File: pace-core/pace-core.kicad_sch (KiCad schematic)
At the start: 3 parts, among them U1 ESP32-S3-WROOM-1

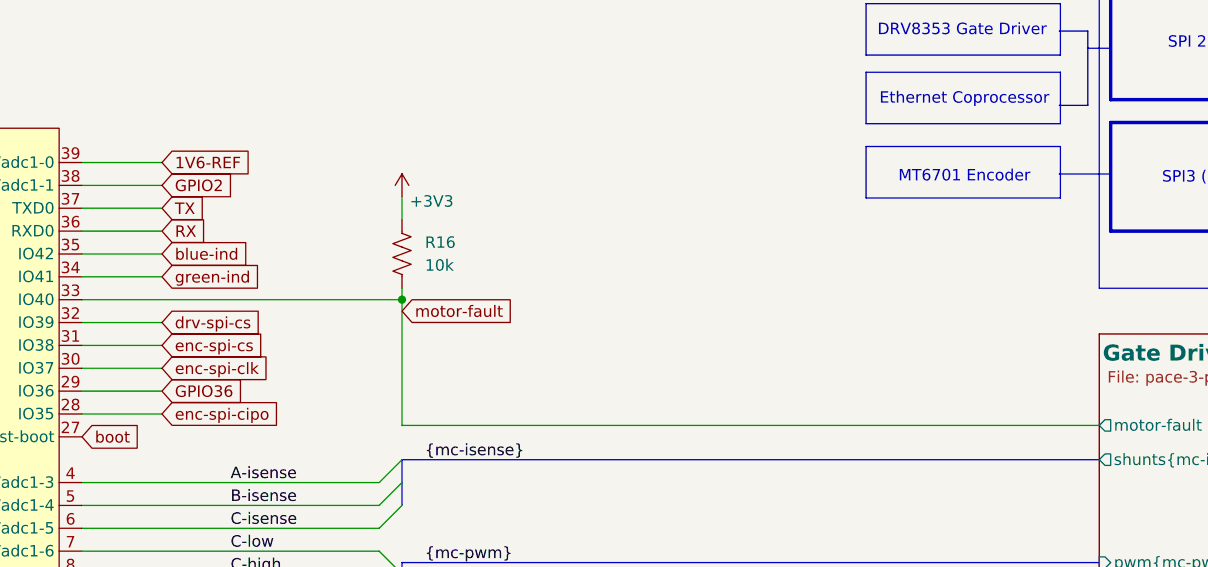
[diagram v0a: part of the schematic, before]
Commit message: design checkpoint: v1 repackage — new connectors, footprints, and layout updates
- Add JST SH/SR series, XT30PW-M, TH cap, and SOT-23-3 footprints with 3D models
- Update connectors, power-reg, and mechanicals schematic sheets
- Rework PCB layout and update board STEP exports (r0 updated, r2 added)
- Regenerate interactive BOM

Co-Authored-By: Claude Fable 5 <noreply@anthropic.com>
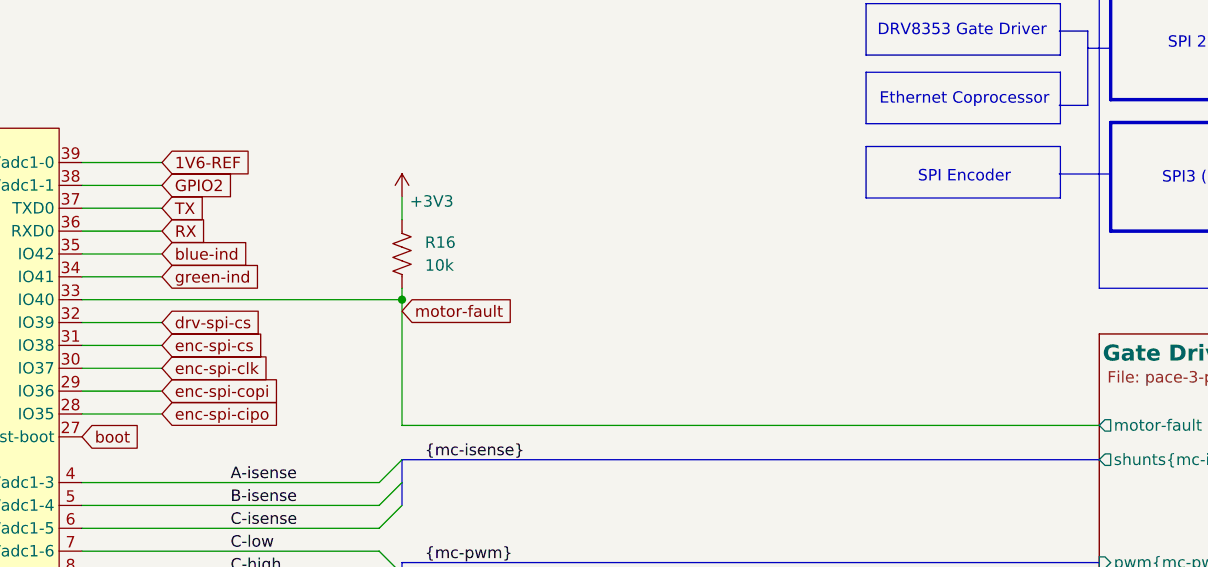
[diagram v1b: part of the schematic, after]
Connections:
- net GPIO36 renamed enc-spi-copi
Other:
- note added: "SPI Encoder"
- note removed: "MT6701 Encoder"
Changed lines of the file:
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@@
 		)
 	)
-	(text "MT6701 Encoder"
+	(text "SPI Encoder"
 		(exclude_from_sim no)
 		(at 184.404 41.021 0)
@@
 		)
 	)
-	(global_label "GPIO36"
+	(global_label "enc-spi-copi"
 		(shape input)
 		(at 95.25 64.77 0)
@@
 		)
 		(property "Intersheetrefs" "${INTERSHEET_REFS}"
-			(at 105.1295 64.77 0)
+			(at 111.4795 64.77 0)
 			(hide yes)
 			(show_name no)

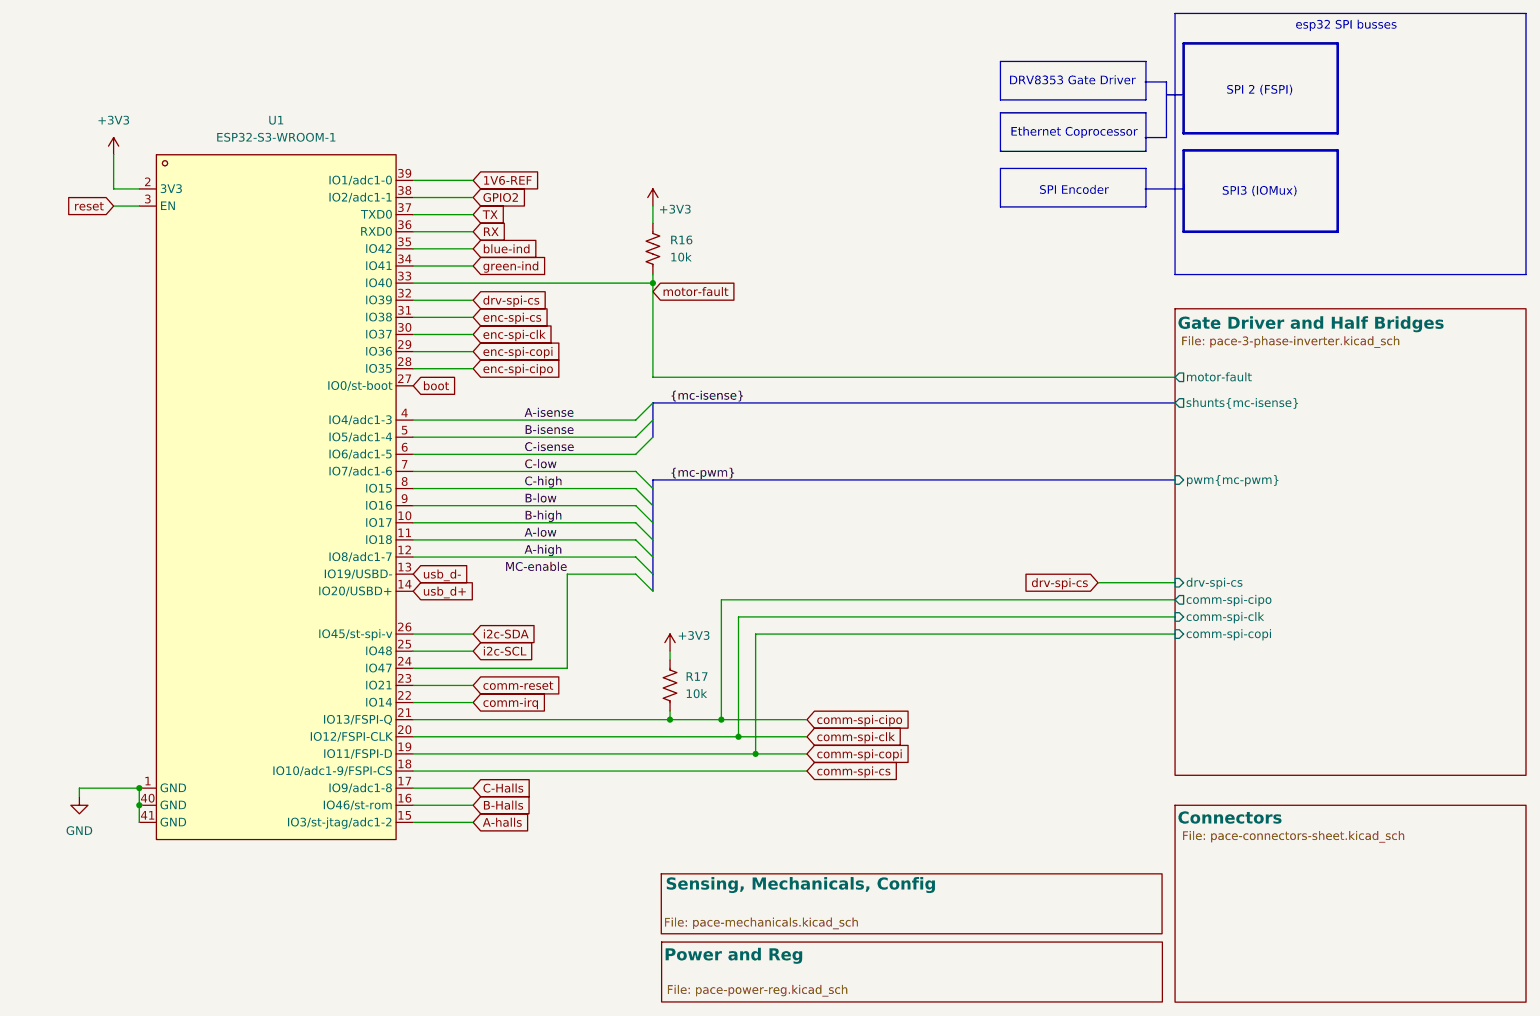
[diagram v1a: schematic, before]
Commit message: Repo hygiene, CI as source of truth, and V1R2 design cleanup
Repository
- Sources only in pace-core/: untrack .history, lock files, .DS_Store,
  backups, layer PDFs, STEP exports, ibom. Regenerable outputs are
  gitignored; CI rebuilds them.
- Git LFS for Blender, PSD, video and curated renders (.gitattributes).
- Move brand artwork to graphics/, curated renders to docs/media/.
- Track the V1R2 fab package CSVs that the old gitignore hid.

CI
- KiBot builds gerbers, drill, fab zip, BOM (CSV/HTML with MPN and LCSC),
  position, ibom, IPC netlist, schematic and layer PDFs, DRC report,
  STEP and renders. REV is set from `git describe` on V*R* tags.
- ERC and DRC block PRs; tag builds publish a GitHub Release.
- README pin map is generated from the netlist (tools/gen_readme.py)
  and checked in CI.
- PR template with review checklist.

Design (ERC 0 errors, DRC 0 errors with schematic parity, netlist
connectivity verified identical across all 101 nets)
- Rename 49 nets to lowercase domain-kebab via tools/rename_nets.py.
- Add TITLE/PROJECT_CODE/REV/COMPANY text variables and title blocks on
  every sheet and the board.
- Net classes now carry both widths and colours: GND, 3V3, 5V, GND-USB,
  Batt, Motor-A/B/C. Remove High-Current-GND (its net never existed).
- Remove all 10 stale DRC exclusions; fold the shunt net-tie bridge copper
  into pad 2 and waive clearance around NT1..NT3 via pace-core.kicad_dru.
- Add Manufacturer/MPN/LCSC fields to every symbol and footprint.
- Fix capacitor symbols with input-typed pins, add PWR_FLAGs on GND and
  +BATT, convert duplicate local labels to global, complete the
  half-bridge bus alias, re-home symbols from missing libraries.

Docs
- docs/style-guide.md, decision records 0001-0003, errata, bring-up
  checklist. CLAUDE.md updated for the new layout and conventions.

Co-Authored-By: Claude Fable 5.1 <noreply@anthropic.com>
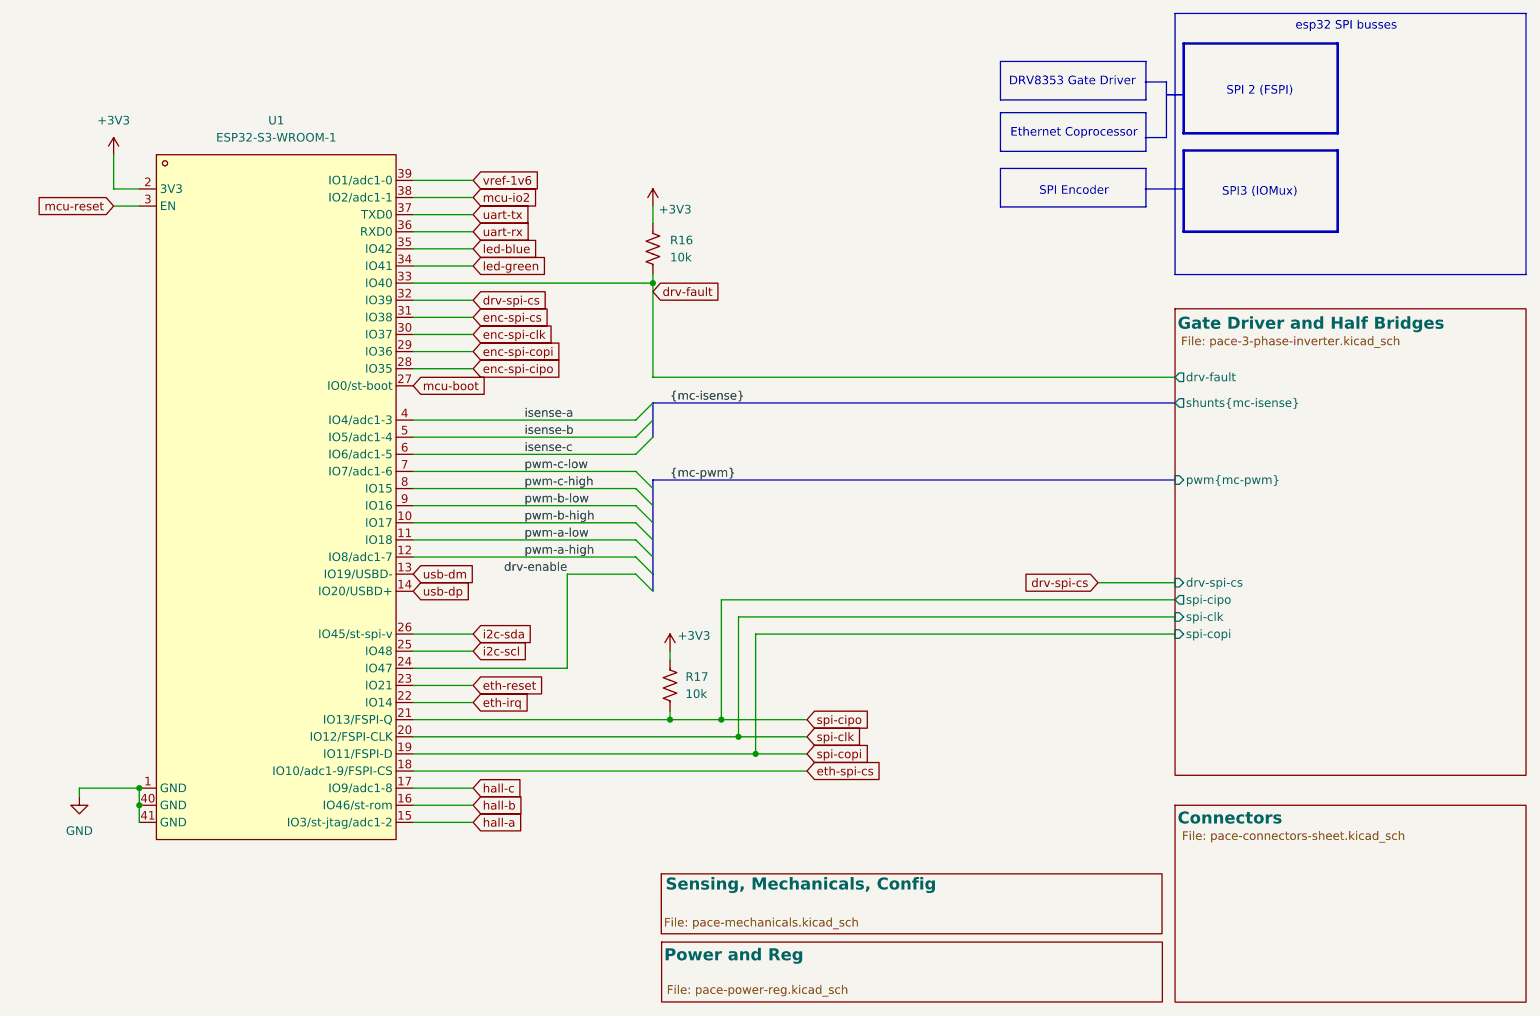
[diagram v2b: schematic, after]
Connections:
- net 1V6-REF renamed vref-1v6
- net A-halls renamed hall-a
- net A-high renamed pwm-a-high
- net A-isense renamed isense-a
- net A-low renamed pwm-a-low
- net B-Halls renamed hall-b
- net B-high renamed pwm-b-high
- net B-isense renamed isense-b
- net B-low renamed pwm-b-low
- net C-Halls renamed hall-c
- net C-high renamed pwm-c-high
- net C-isense renamed isense-c
- net C-low renamed pwm-c-low
- net GPIO2 renamed mcu-io2
- net MC-enable renamed drv-enable
- net RX renamed uart-rx
- net TX renamed uart-tx
- net blue-ind renamed led-blue
- net boot renamed mcu-boot
- net comm-irq renamed eth-irq
- net comm-reset renamed eth-reset
- net comm-spi-cipo renamed spi-cipo
- net comm-spi-clk renamed spi-clk
- net comm-spi-copi renamed spi-copi
- net comm-spi-cs renamed eth-spi-cs
- net green-ind renamed led-green
- net i2c-SCL renamed i2c-scl
- net i2c-SDA renamed i2c-sda
- net motor-fault renamed drv-fault
- net reset renamed mcu-reset
- net usb_d+ renamed usb-dp
- net usb_d- renamed usb-dm
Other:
- sheet Gate Driver and Half Bridges ports: added drv-fault, spi-cipo, spi-clk, spi-copi; removed comm-spi-cipo, comm-spi-clk, comm-spi-copi, motor-fault
- company: (none) -> ${COMPANY}
- title: (none) -> ${TITLE} - System
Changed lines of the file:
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@@
 	(generator_version "10.0")
 	(paper "A4")
+	(title_block
+		(title "${TITLE} - System")
+		(date "2026-09-30")
+		(rev "${REV}")
+		(company "${COMPANY}")
+		(comment 1 "Root sheet: ESP32-S3 MCU, sheet interconnect, pin allocation")
+		(comment 2 "Project code ${PROJECT_CODE}")
+	)
 	(rectangle
 		(start 200.66 19.05)
@@
 		)
 	)
-	(label "A-isense"
+	(label "isense-a"
 		(at 102.87 74.93 0)
 		(effects
@@
 		)
 	)
-	(label "B-isense"
+	(label "isense-b"
 		(at 102.87 77.47 0)
 		(effects
@@
 		)
 	)
-	(label "C-isense"
+	(label "isense-c"
 		(at 102.87 80.01 0)
 		(effects
@@
 		)
 	)
-	(label "A-low"
+	(label "pwm-a-low"
 		(at 102.87 92.71 0)
 		(effects
@@
 		)
 	)
-	(label "C-high"
+	(label "pwm-c-high"
 		(at 102.87 85.09 0)
 		(effects
@@
 		)
 	)
-	(label "C-low"
+	(label "pwm-c-low"
 		(at 102.87 82.55 0)
 		(effects
@@
 		)
 	)
-	(label "A-high"
+	(label "pwm-a-high"
 		(at 102.87 95.25 0)
 		(effects
@@
 		)
 	)
-	(label "MC-enable"
+	(label "drv-enable"
 		(at 109.22 97.79 180)
 		(effects
@@
 		)
 	)
-	(label "B-low"
+	(label "pwm-b-low"
 		(at 102.87 87.63 0)
 		(effects
@@
 		)
 	)
-	(label "B-high"
+	(label "pwm-b-high"
 		(at 102.87 90.17 0)
 		(effects
@@
 		)
 	)
-	(global_label "green-ind"
+	(global_label "led-green"
 		(shape input)
 		(at 95.25 52.07 0)
@@
 		)
 	)
-	(global_label "comm-spi-clk"
+	(global_label "spi-clk"
 		(shape input)
 		(at 144.78 121.92 0)
@@
 		)
 	)
-	(global_label "RX"
+	(global_label "uart-rx"
 		(shape input)
 		(at 95.25 46.99 0)
@@
 		)
 	)
-	(global_label "comm-spi-cipo"
+	(global_label "spi-cipo"
 		(shape input)
 		(at 144.78 119.38 0)
@@
 		)
 	)
-	(global_label "comm-reset"
+	(global_label "eth-reset"
 		(shape input)
 		(at 95.25 114.3 0)
@@
 		)
 	)
-	(global_label "comm-spi-cs"
+	(global_label "eth-spi-cs"
 		(shape input)
 		(at 144.78 127 0)
@@
 		)
 	)
-	(global_label "TX"
+	(global_label "uart-tx"
 		(shape input)
 		(at 95.25 44.45 0)
@@
 		)
 	)
-	(global_label "boot"
+	(global_label "mcu-boot"
 		(shape input)
 		(at 86.36 69.85 0)
@@
 		)
 	)
-	(global_label "B-Halls"
+	(global_label "hall-b"
 		(shape input)
 		(at 95.25 132.08 0)
@@
 		)
 	)
-	(global_label "usb_d+"
+	(global_label "usb-dp"
 		(shape input)
 		(at 86.36 100.33 0)
@@
 		)
 	)
-	(global_label "motor-fault"
+	(global_label "drv-fault"
 		(shape input)
 		(at 121.92 55.88 0)
@@
 		)
 	)
-	(global_label "reset"
+	(global_label "mcu-reset"
 		(shape input)
 		(at 41.91 43.18 180)
@@
 		)
 	)
-	(global_label "GPIO2"
+	(global_label "mcu-io2"
 		(shape input)
 		(at 95.25 41.91 0)
@@
 		)
 	)
-	(global_label "usb_d-"
+	(global_label "usb-dm"
 		(shape input)
 		(at 86.36 97.79 0)
@@
 		)
 	)
-	(global_label "A-halls"
+	(global_label "hall-a"
 		(shape input)
 		(at 95.25 134.62 0)
@@
 		)
 	)
-	(global_label "1V6-REF"
+	(global_label "vref-1v6"
 		(shape input)
 		(at 95.25 39.37 0)
@@
 		)
 	)
-	(global_label "i2c-SDA"
+	(global_label "i2c-sda"
 		(shape input)
 		(at 95.25 106.68 0)
@@
 		)
 	)
-	(global_label "comm-irq"
+	(global_label "eth-irq"
 		(shape input)
 		(at 95.25 116.84 0)
@@
 		)
 	)
-	(global_label "blue-ind"
+	(global_label "led-blue"
 		(shape input)
 		(at 95.25 49.53 0)
@@
 		)
 	)
-	(global_label "C-Halls"
+	(global_label "hall-c"
 		(shape input)
 		(at 95.25 129.54 0)
@@
 		)
 	)
-	(global_label "comm-spi-copi"
+	(global_label "spi-copi"
 		(shape input)
 		(at 144.78 124.46 0)
@@
 		)
 	)
-	(global_label "i2c-SCL"
+	(global_label "i2c-scl"
 		(shape input)
 		(at 95.25 109.22 0)
@@
 			)
 		)
+		(property "Manufacturer" ""
+			(at 121.92 49.53 0)
+			(show_name no)
+			(do_not_autoplace no)
+			(effects
+				(font
+					(size 1.27 1.27)
+				)
+				(hide yes)
+			)
+		)
+		(property "MPN" ""
+			(at 121.92 49.53 0)
+			(show_name no)
+			(do_not_autoplace no)
+			(effects
+				(font
+					(size 1.27 1.27)
+				)
+				(hide yes)
+			)
+		)
+		(property "LCSC Part" ""
+			(at 121.92 49.53 0)
+			(show_name no)
+			(do_not_autoplace no)
+			(effects
+				(font
+					(size 1.27 1.27)
+				)
+				(hide yes)
+			)
+		)
 		(property "Description" "Resistor, US symbol"
 			(at 121.92 49.53 0)
@@
 			)
 		)
+		(property "Manufacturer" ""
+			(at 124.46 114.3 0)
+			(show_name no)
+			(do_not_autoplace no)
+			(effects
+				(font
+					(size 1.27 1.27)
+				)
+				(hide yes)
+			)
+		)
+		(property "MPN" ""
+			(at 124.46 114.3 0)
+			(show_name no)
+			(do_not_autoplace no)
+			(effects
+				(font
+					(size 1.27 1.27)
+				)
+				(hide yes)
+			)
+		)
+		(property "LCSC Part" ""
+			(at 124.46 114.3 0)
+			(show_name no)
+			(do_not_autoplace no)
+			(effects
+				(font
+					(size 1.27 1.27)
+				)
+				(hide yes)
+			)
+		)
 		(property "Description" "Resistor, US symbol"
 			(at 124.46 114.3 0)
@@
 			)
 		)
-		(pin "comm-spi-cipo" output
+		(pin "spi-cipo" output
 			(at 199.39 101.6 180)
 			(effects
@@
 			)
 		)
-		(pin "comm-spi-clk" input
+		(pin "spi-clk" input
 			(at 199.39 104.14 180)
 			(effects
@@
 			)
 		)
-		(pin "comm-spi-copi" input
+		(pin "spi-copi" input
 			(at 199.39 106.68 180)
 			(effects
@@
 			)
 		)
-		(pin "motor-fault" output
+		(pin "drv-fault" output
 			(at 199.39 68.58 180)
 			(effects
